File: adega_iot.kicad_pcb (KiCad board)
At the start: 2 copper layers, 100 x 100 mm, 90 parts, among them J1 Conn_01x03_Pin, J10 Conn_01x02_Pin, J2 Conn_01x02_Pin, J3 Screw_Terminal_01x02, J4 Conn_01x03_Pin, J6 Conn_01x03_Pin, J7 Screw_Terminal_01x02, J8 Conn_01x02_Pin, J9 Conn_01x02_Pin, Q1 BC548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

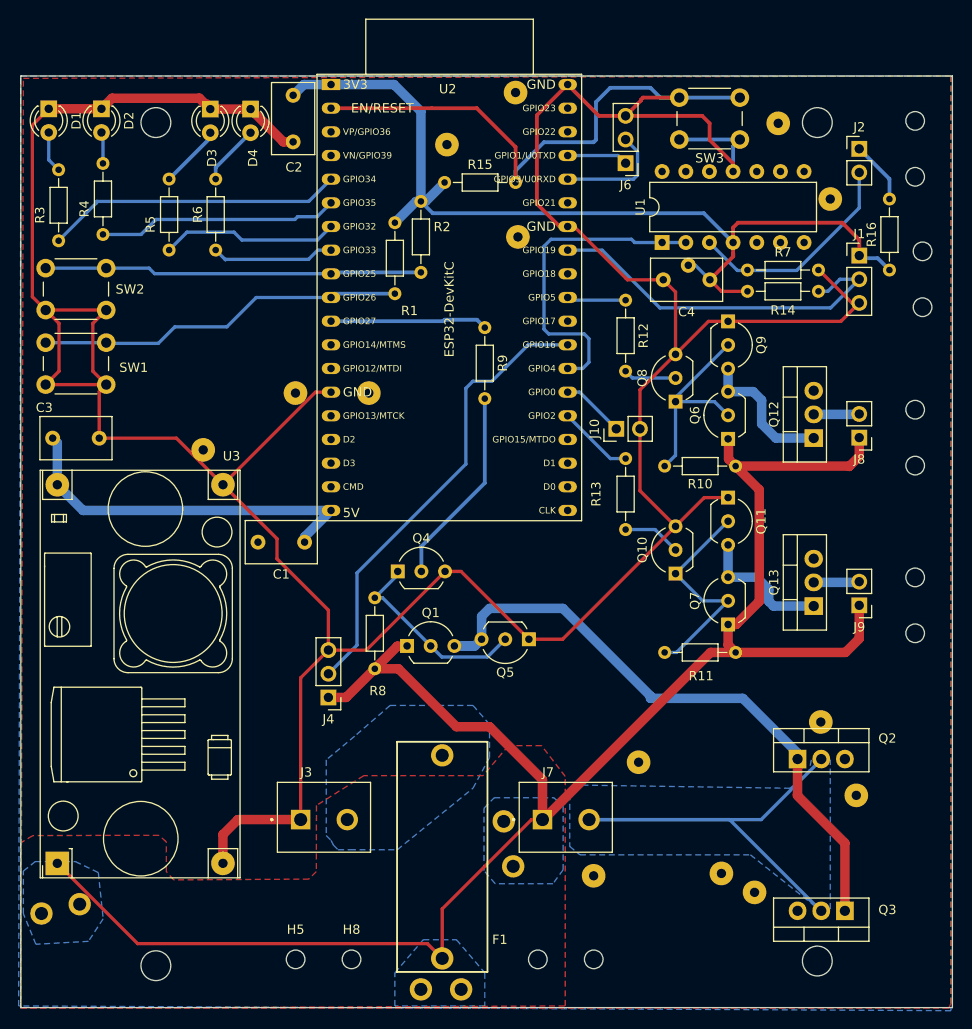
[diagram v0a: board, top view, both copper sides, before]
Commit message: Added Thermistor on GPIO pin
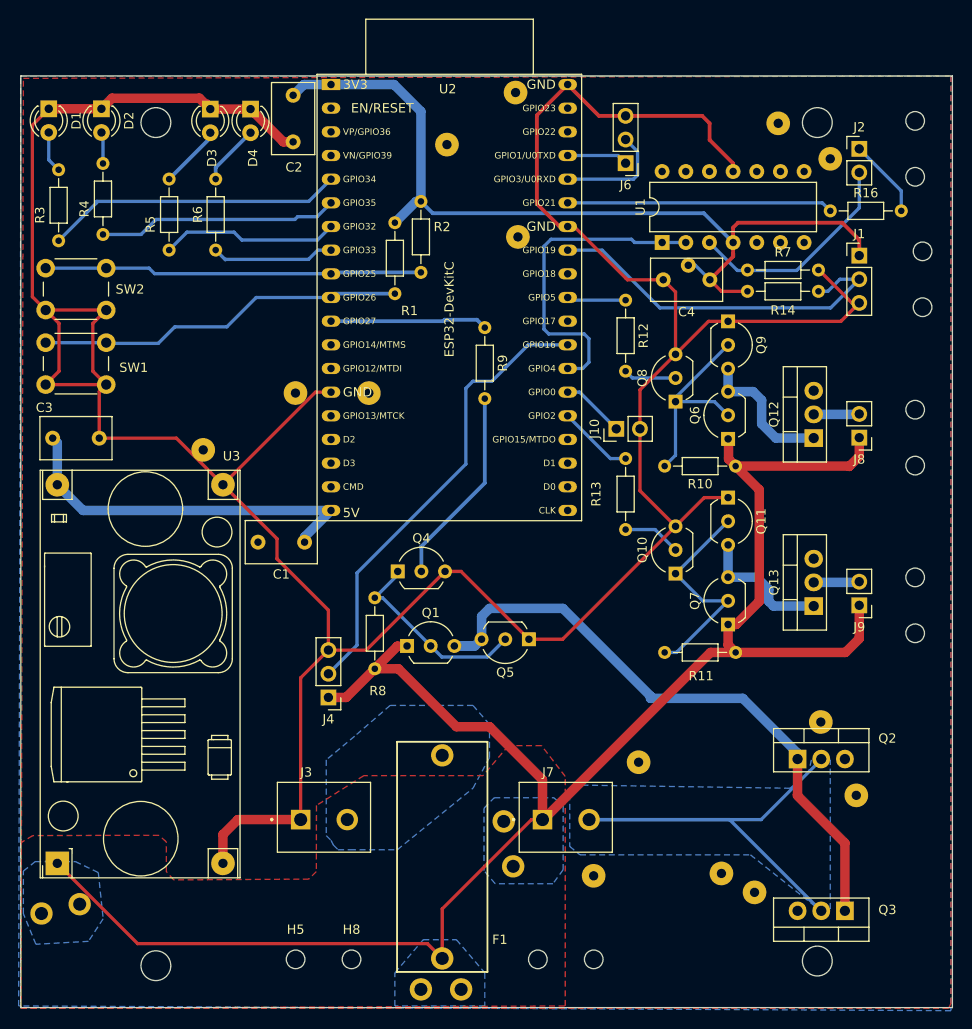
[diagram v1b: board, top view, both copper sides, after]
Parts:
- removed R15: 10k, Resistor_THT:R_Axial_DIN0204_L3.6mm_D1.6mm_P7.62mm_Horizontal
- removed SW3: SW_Push, Button_Switch_THT:SW_PUSH_6mm_H7.3mm
- moved R16 8.98 mm to (86.9, 14.5), turned to 0 degrees
- moved ? 4.32 mm to (86.9, 8.89)
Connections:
- R16 pad 1: +3V3 -> /THERMISTOR_ON
- U2 pad 2: /RST -> unconnected-(U2-CHIP_PU-Pad2)
- U2 pad 33: unconnected-(U2-GPIO21-Pad33) -> /THERMISTOR_ON
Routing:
- net /RST: track 57.2 -> 0.00 mm
- net /THERMISTOR_ON: track 0.00 -> 28.5 mm
- net GND: track 377.7 -> 360.8 mm
- net +3V3: track 102.3 -> 95.0 mm
- net Net-(J2-Pin_1): track 6.73 -> 8.53 mm

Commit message: bug fixes
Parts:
- removed J10: Conn_01x02_Pin, Connector_PinHeader_2.54mm:PinHeader_1x02_P2.54mm_Vertical
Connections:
- U2 pad 25: /BOOT -> unconnected-(U2-GPIO0/BOOT/ADC2_CH1-Pad25)
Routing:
- net /BOOT: track 6.85 -> 0.00 mm
